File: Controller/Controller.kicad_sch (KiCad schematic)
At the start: 66 parts, among them J1 Prog, J2 PWR, Q1 BC547, Q2 BC547, Q3 IRF5305, SW1 Flash, SW2 Reset, U1 ESP-12E, U2 MCP3208, U3 LM324, U4 LM393

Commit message: Refine voltage generation and add connectors
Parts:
- removed C16: 4u7, Package_LCC:PLCC-44_16.6x16.6mm_P1.27mm, symbol Device:C_Polarized
- removed J2: PWR, symbol Connector:Conn_01x04_Pin
- added C19: 4u7, Package_LCC:PLCC-44_16.6x16.6mm_P1.27mm, symbol Device:C_Polarized
- added C20, C21: 100n, symbol Device:C
- added J3: PWR, symbol Connector:Conn_01x02_Socket
- added J4: Heater, symbol Connector:Conn_01x02_Socket
- added J5: Pololu reg16a 3V3, symbol Connector:Conn_01x04_Socket
- added U5: LM78L05_TO92, Package_TO_SOT_THT:TO-92_Inline, symbol Regulator_Linear:LM78L05_TO92
- C2: value 33u -> 47u
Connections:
- net +24V: now also C2.1, C19.1, C21.1, J3.2 (Pin_2), J5.2 (Pin_2), U5.3 (VI)
- net +3V3: now also J5.4 (Pin_4); no longer C2.1
- net +5V: now also C20.1, U5.1 (VO)
- net GND: now also C19.2, C20.2, C21.2, J3.1 (Pin_1), J5.3 (Pin_3), U5.2 (GND)
- net HEATER_NEG: now also J4.2 (Pin_2)
- net HEATER_POS: now also J4.1 (Pin_1)
- no-connect marks 7 -> 8
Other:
- moved on the sheet: C12, C2, J1, SW1, SW2, U4C

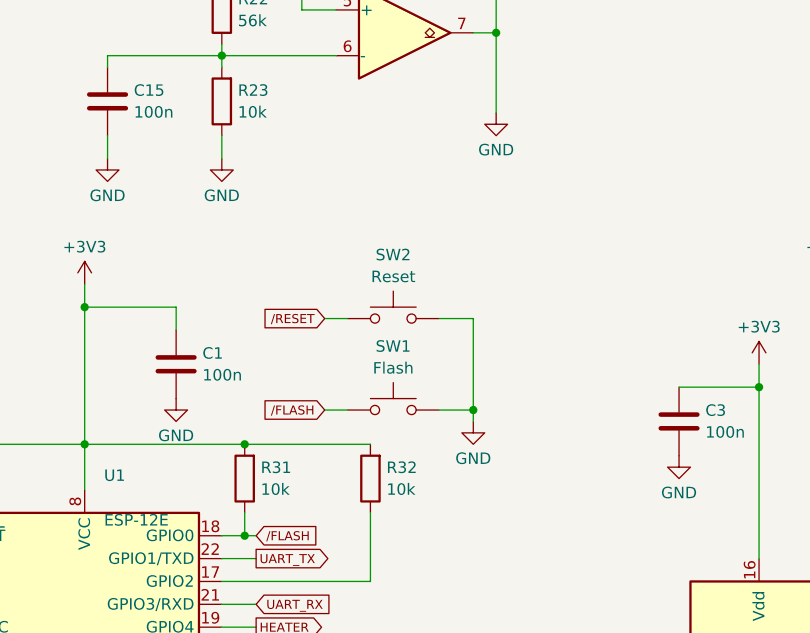
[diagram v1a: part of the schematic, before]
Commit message: Assign footprints
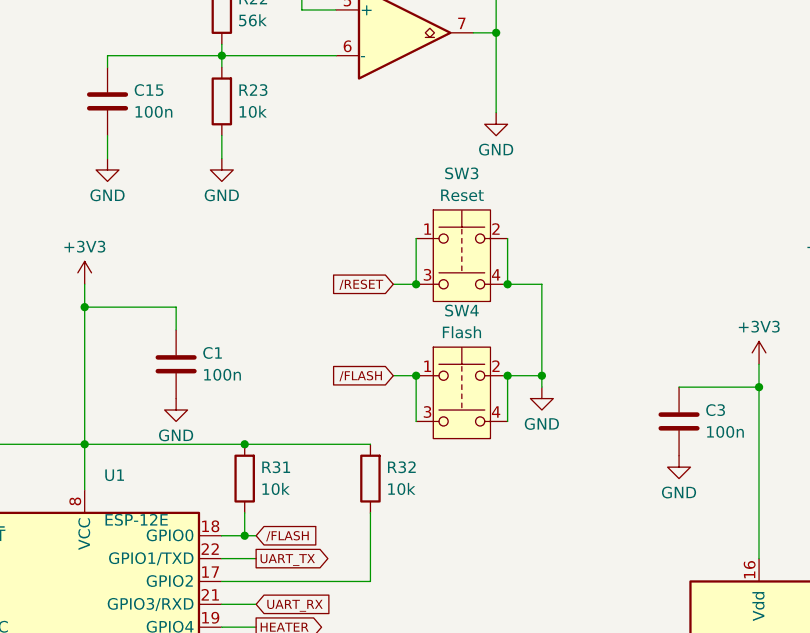
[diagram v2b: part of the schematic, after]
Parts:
- removed SW1: Flash, Package_TO_SOT_SMD:TO-263-7_TabPin8, symbol Switch:SW_Push
- removed SW2: Reset, Package_TO_SOT_SMD:TO-263-7_TabPin8, symbol Switch:SW_Push
- added SW3: Reset, Button_Switch_THT:SW_DIP_SPSTx02_Slide_6.7x6.64mm_W7.62mm_P2.54mm_LowProfile, symbol Switch:SW_Push_Dual
- added SW4: Flash, Button_Switch_THT:SW_DIP_SPSTx02_Slide_6.7x6.64mm_W7.62mm_P2.54mm_LowProfile, symbol Switch:SW_Push_Dual
- C1, C10, C11, C12, C13, C14, C15, C18, C20, C21, C3, C4, C5, C6, C7, C8, C9: footprint (none) -> Capacitor_THT:C_Disc_D4.3mm_W1.9mm_P5.00mm
- C17, C19: footprint Package_LCC:PLCC-44_16.6x16.6mm_P1.27mm -> Capacitor_THT:CP_Radial_D4.0mm_P1.50mm
- C2: footprint Package_LCC:PLCC-44_16.6x16.6mm_P1.27mm -> Capacitor_THT:CP_Radial_D6.3mm_P2.50mm
- D1: footprint (none) -> Diode_THT:D_DO-41_SOD81_P7.62mm_Horizontal
- F1: footprint (none) -> Fuse:Fuseholder_Cylinder-5x20mm_Stelvio-Kontek_PTF78_Horizontal_Open
- J1: footprint LED_THT:LED_D5.0mm_IRGrey -> Connector_PinHeader_2.54mm:PinHeader_1x06_P2.54mm_Vertical
- J3, J4: footprint (none) -> Connector_JST:JST_NV_B02P-NV_1x02_P5.00mm_Vertical
- J5: footprint (none) -> Connector_PinSocket_2.54mm:PinSocket_1x04_P2.54mm_Vertical
- R1, R10, R11, R12, R13, R14, R15, R16, R17, R18, R19, R2, R20, R21, R22, R23, R24, R25, R27, R28, R29, R3, R30, R31, R32, R4, R5, R6, R7, R8: footprint (none) -> Resistor_THT:R_Axial_DIN0207_L6.3mm_D2.5mm_P7.62mm_Horizontal
- R26: footprint (none) -> Resistor_THT:R_Axial_DIN0614_L14.3mm_D5.7mm_P15.24mm_Horizontal
- U3: footprint (none) -> Package_DIP:DIP-14_W7.62mm_LongPads
- U4: footprint (none) -> Package_DIP:DIP-8_W7.62mm_LongPads
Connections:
- net GND: now also SW3.2, SW3.4, SW4.2, SW4.4
- net /FLASH: now also SW4.1, SW4.3
- net /RESET: now also SW3.1, SW3.3

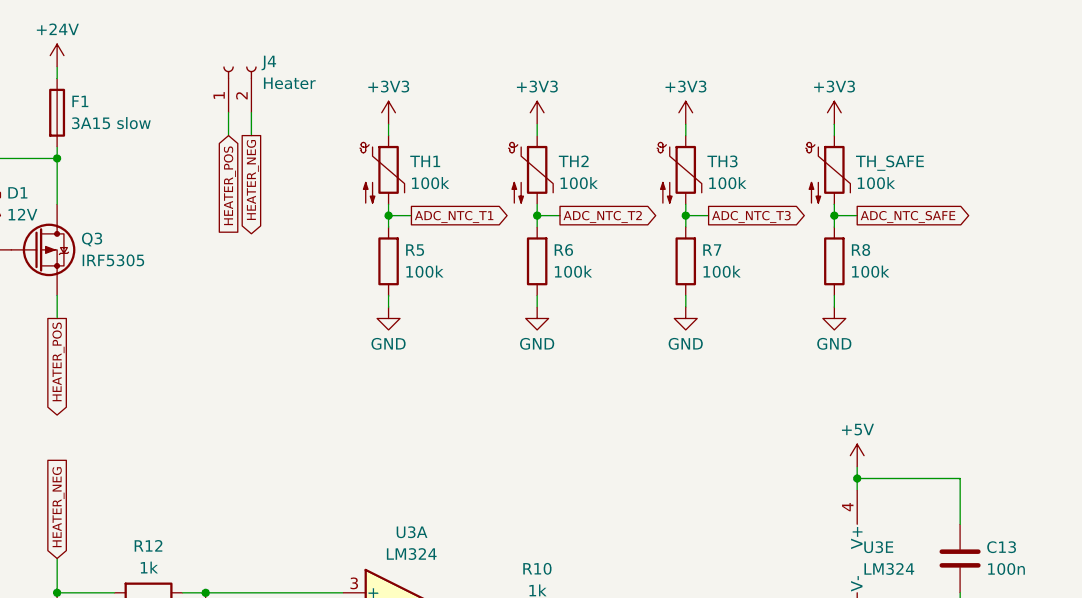
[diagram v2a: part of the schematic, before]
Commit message: Add connector for NTCs
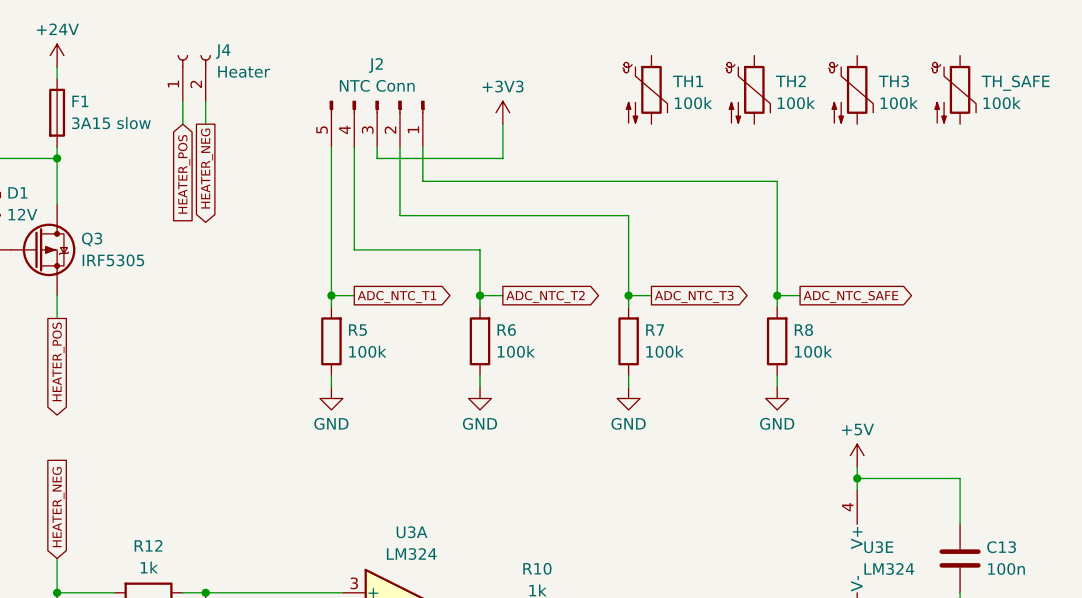
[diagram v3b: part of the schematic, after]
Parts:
- added J2: NTC Conn, Connector_JST:JST_EH_B5B-EH-A_1x05_P2.50mm_Vertical, symbol Connector:Conn_01x05_Pin
- TH1, TH2, TH3, TH_SAFE: now left out of the parts list
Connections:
- net +3V3: now also J2.3 (Pin_3); no longer TH1.1, TH2.1, TH3.1, TH_SAFE.1
- net ADC_NTC_SAFE: now also J2.1 (Pin_1); no longer TH_SAFE.2
- net ADC_NTC_T1: now also J2.5 (Pin_5); no longer TH1.2
- net ADC_NTC_T2: now also J2.4 (Pin_4); no longer TH2.2
- net ADC_NTC_T3: now also J2.2 (Pin_2); no longer TH3.2
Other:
- moved on the sheet: J4, R5, R6, R7, R8, TH1, TH2, TH3, TH_SAFE

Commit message: First attempt on board layout
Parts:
- removed Q3: IRF5305, Package_TO_SOT_SMD:SOT-23, symbol Device:Q_PMOS_Depletion
- added D2: gn, LED_THT:LED_D3.0mm, symbol Device:LED
- added Q3: IRF5305, Package_TO_SOT_THT:TO-220-3_Vertical, symbol Device:Q_PMOS
- added R33: 470R, Resistor_THT:R_Axial_DIN0207_L6.3mm_D2.5mm_P7.62mm_Horizontal, symbol Device:R
- U2: footprint Package_DFN_QFN:QFN-20-1EP_5x5mm_P0.65mm_EP3.35x3.35mm -> Package_DIP:DIP-16_W7.62mm_LongPads
- renumbered TH_SAFE to TH_SAFE1
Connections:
- net +24V: now also R33.2
- net GND: now also D2.1 (K); no longer R17.2, R24.1, R25.1, U1.4 (GPIO16), U4.1, U4.7
- net HEATER_POS: now also Q3.3 (S)
- net at D1.1 (K), F1.2, R15.2: now also Q3.2 (D)
- net at D1.2 (A), R15.1, R16.2: now also Q3.1 (G)
- new net: D2.2 (A), R33.1
- new net SAFETY_OK: R17.2, R24.1, R25.1, U1.4 (GPIO16), U4.1, U4.7
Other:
- moved on the sheet: C2, J5

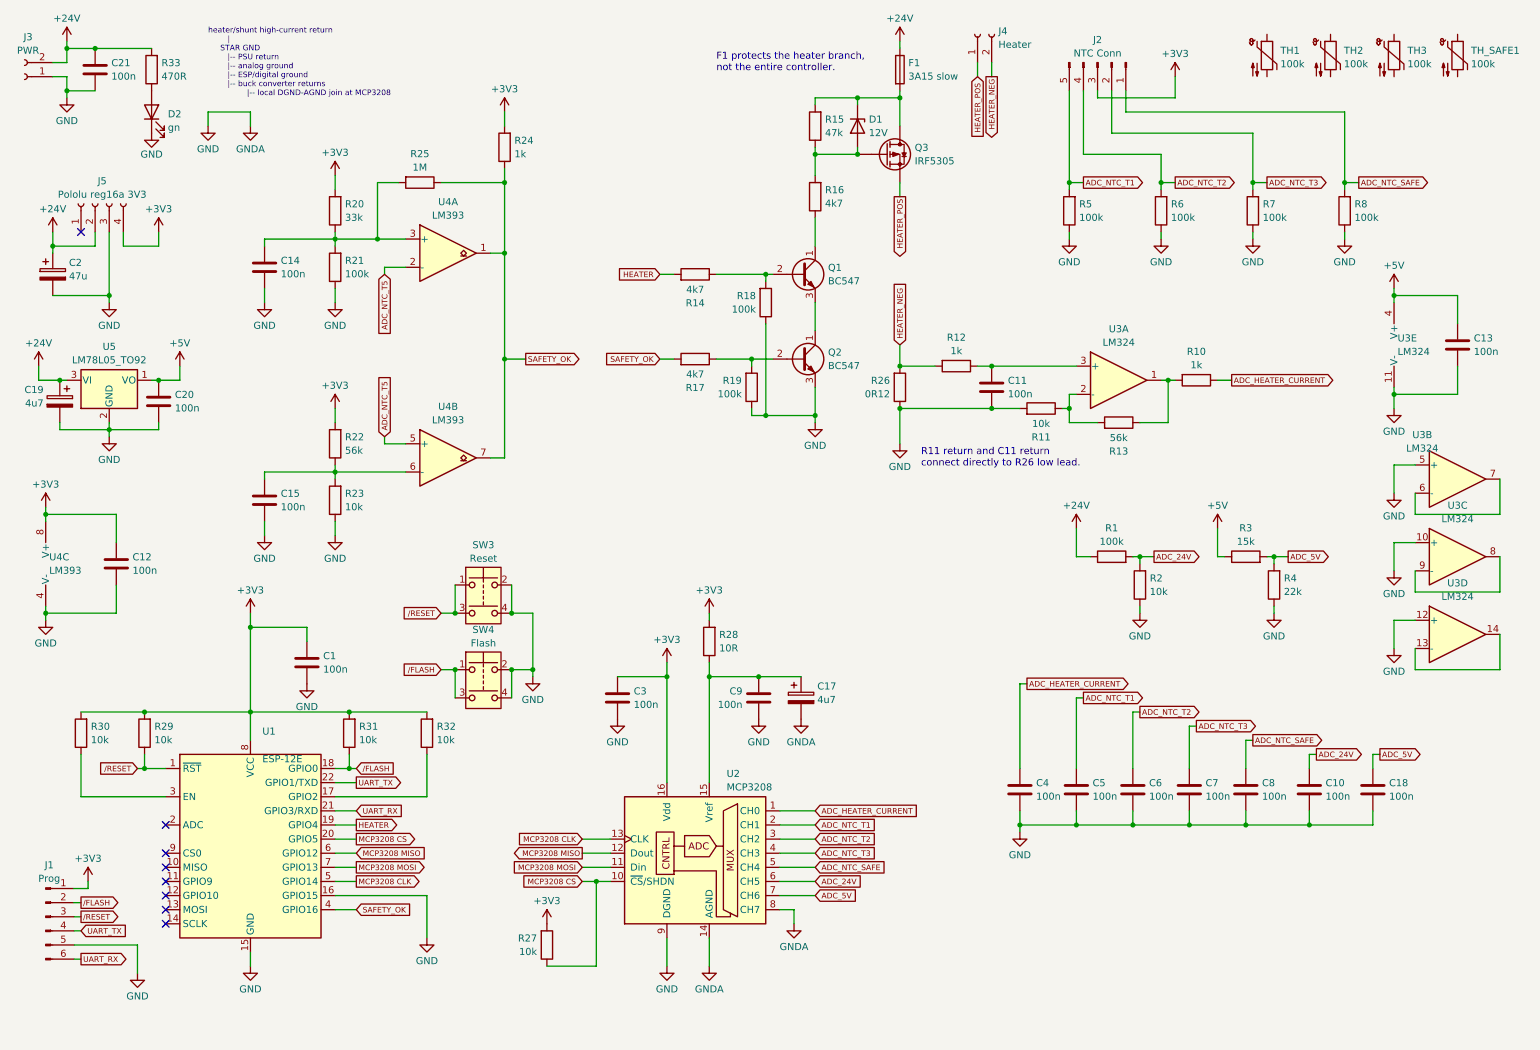
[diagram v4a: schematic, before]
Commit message: Switch to Teensy Pro Micro
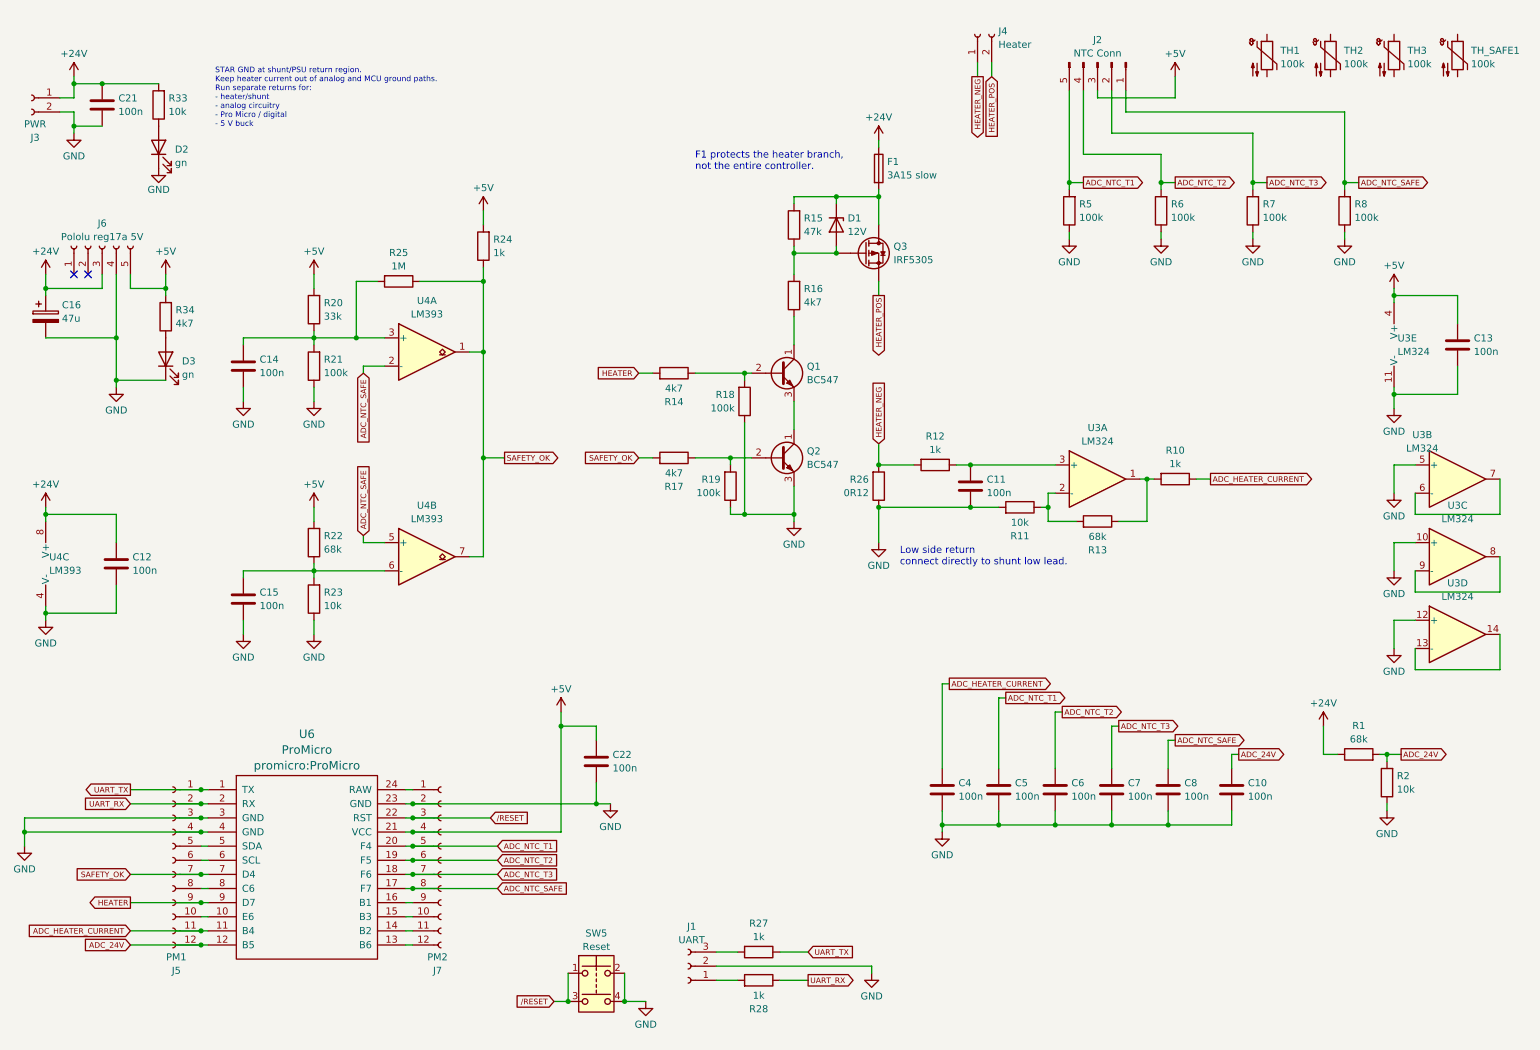
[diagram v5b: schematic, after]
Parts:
- removed C1, C18, C20, C3, C9: 100n, Capacitor_THT:C_Disc_D4.3mm_W1.9mm_P5.00mm, symbol Device:C
- removed C17, C19: 4u7, Capacitor_THT:CP_Radial_D4.0mm_P1.50mm, symbol Device:C_Polarized
- removed C2: 47u, Capacitor_THT:CP_Radial_D6.3mm_P2.50mm, symbol Device:C_Polarized
- removed J1: Prog, Connector_PinHeader_2.54mm:PinHeader_1x06_P2.54mm_Vertical, symbol Connector:Conn_01x06_Pin
- removed J5: Pololu reg16a 3V3, Connector_PinSocket_2.54mm:PinSocket_1x04_P2.54mm_Vertical, symbol Connector:Conn_01x04_Socket
- removed R29, R30, R31, R32: 10k, Resistor_THT:R_Axial_DIN0207_L6.3mm_D2.5mm_P7.62mm_Horizontal, symbol Device:R
- removed R3: 15k, Resistor_THT:R_Axial_DIN0207_L6.3mm_D2.5mm_P7.62mm_Horizontal, symbol Device:R
- removed R4: 22k, Resistor_THT:R_Axial_DIN0207_L6.3mm_D2.5mm_P7.62mm_Horizontal, symbol Device:R
- removed SW3: Reset, Button_Switch_THT:SW_DIP_SPSTx02_Slide_6.7x6.64mm_W7.62mm_P2.54mm_LowProfile, symbol Switch:SW_Push_Dual
- removed SW4: Flash, Button_Switch_THT:SW_DIP_SPSTx02_Slide_6.7x6.64mm_W7.62mm_P2.54mm_LowProfile, symbol Switch:SW_Push_Dual
- removed U1: ESP-12E, RF_Module:ESP-12E, symbol RF_Module:ESP-12E
- removed U2: MCP3208, Package_DIP:DIP-16_W7.62mm_LongPads, symbol Analog_ADC:MCP3208
- removed U5: LM78L05_TO92, Package_TO_SOT_THT:TO-92_Inline, symbol Regulator_Linear:LM78L05_TO92
- added C16: 47u, Capacitor_THT:CP_Radial_D6.3mm_P2.50mm, symbol Device:C_Polarized
- added C22: 100n, Capacitor_THT:C_Disc_D4.3mm_W1.9mm_P5.00mm, symbol Device:C
- added D3: gn, LED_THT:LED_D3.0mm, symbol Device:LED
- added J1: UART, Connector_PinHeader_2.54mm:PinHeader_1x03_P2.54mm_Vertical, symbol Connector:Conn_01x03_Socket
- added J5: PM1, Connector_PinSocket_2.54mm:PinSocket_1x12_P2.54mm_Vertical, symbol Connector:Conn_01x12_Socket
- added J6: Pololu reg17a 5V, Connector_PinHeader_2.54mm:PinHeader_1x05_P2.54mm_Vertical, symbol Connector:Conn_01x05_Socket
- added J7: PM2, Connector_PinSocket_2.54mm:PinSocket_1x12_P2.54mm_Vertical, symbol Connector:Conn_01x12_Socket
- added R34: 4k7, Resistor_THT:R_Axial_DIN0207_L6.3mm_D2.5mm_P7.62mm_Horizontal, symbol Device:R
- added SW5: Reset, Button_Switch_THT:SW_DIP_SPSTx02_Slide_6.7x6.64mm_W7.62mm_P2.54mm_LowProfile, symbol Switch:SW_Push_Dual
- added U6: ProMicro, promicro:ProMicro, symbol promicro:ProMicro
- R1: value 100k -> 68k
- R13, R22: value 56k -> 68k
- R27: value 10k -> 1k
- R28: value 10R -> 1k
- R33: value 470R -> 10k
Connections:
- net ADC_NTC_T5 is gone; now on net ADC_NTC_SAFE: U4.2 (-), U4.5 (+)
- net MCP3208 CS is gone; now on net UART_TX: R27.1
- net +24V: now also C12.1, J3.1 (Pin_1), U4.8 (V+), C16.1, J6.3 (Pin_3); no longer J3.2 (Pin_2)
- net +5V: now also J2.3 (Pin_3), R20.2, R22.2, R24.2, C22.1, J6.5 (Pin_5), J7.4 (Pin_4), R34.2, U6.21 (VCC)
- net ADC_24V: now also J5.12 (Pin_12), U6.12 (B5)
- net ADC_HEATER_CURRENT: now also J5.11 (Pin_11), U6.11 (B4)
- net ADC_NTC_SAFE: now also J7.8 (Pin_8), U6.17 (F7)
- net ADC_NTC_T1: now also J7.5 (Pin_5), U6.20 (F4)
- net ADC_NTC_T2: now also J7.6 (Pin_6), U6.19 (F5)
- net ADC_NTC_T3: now also J7.7 (Pin_7), U6.18 (F6)
- net GND: now also J3.2 (Pin_2), C16.2, C22.2, D3.1 (K), J1.2 (Pin_2), J5.3 (Pin_3), J5.4 (Pin_4), J6.4 (Pin_4), J7.2 (Pin_2), SW5.2, SW5.4, U6.23 (GND), U6.3 (GND), U6.4 (GND); no longer J3.1 (Pin_1)
- net HEATER: now also J5.9 (Pin_9), U6.9 (D7)
- net HEATER_NEG: now also J4.1 (Pin_1); no longer J4.2 (Pin_2)
- net HEATER_POS: now also J4.2 (Pin_2); no longer J4.1 (Pin_1)
- net SAFETY_OK: now also J5.7 (Pin_7), U6.7 (D4)
- net UART_RX: now also R28.1, J5.2 (Pin_2), U6.2 (RX)
- net UART_TX: now also J5.1 (Pin_1), U6.1 (TX)
- net /RESET: now also J7.3 (Pin_3), SW5.1, SW5.3, U6.22 (RST)
- removed net +3V3: C12.1, J2.3 (Pin_3), R20.2, R22.2, R24.2, R27.2, R28.2, U4.8 (V+)
- new net: J5.10 (Pin_10), U6.10 (E6)
- new net: J7.12 (Pin_12), U6.13 (B6)
- new net: J7.11 (Pin_11), U6.14 (B2)
- new net: J7.10 (Pin_10), U6.15 (B3)
- new net: J7.9 (Pin_9), U6.16 (B1)
- new net: J7.1 (Pin_1), U6.24 (RAW)
- new net: J5.5 (Pin_5), U6.5 (SDA)
- new net: J5.6 (Pin_6), U6.6 (SCL)
- new net: J5.8 (Pin_8), U6.8 (C6)
- new net: J1.1 (Pin_1), R28.2
- new net: J1.3 (Pin_3), R27.2
- new net: D3.2 (A), R34.1
- no-connect marks 8 -> 2
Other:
- note added: "Low side return connect directly to shunt low lead."
- note added: "STAR GND at shunt/PSU return region. Keep heater current out of analog and MCU ground paths. Run separate returns for: - heater/shunt - analog circuitry - Pro Micro / digital - 5 V buck"
- note removed: "R11 return and C11 return connect directly to R26 low lead."
- note removed: "heater/shunt high-current return | STAR GND |-- PSU return |-- analog ground |-- ESP/digital ground |-- buck converter returns |-- local DGND-AGND join at MCP3208"
- moved on the sheet: C10, C11, C14, C15, C21, C4, C5, C6, C7, C8, D1, D2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
